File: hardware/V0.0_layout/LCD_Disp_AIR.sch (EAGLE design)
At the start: 41 parts, among them IC3 TC10553.3V, J1 12V input, Q1 16MHz, SW1 ENCODER_SW1-PEC12, U1 ATMEGA328P-AU(R), U3 78M05

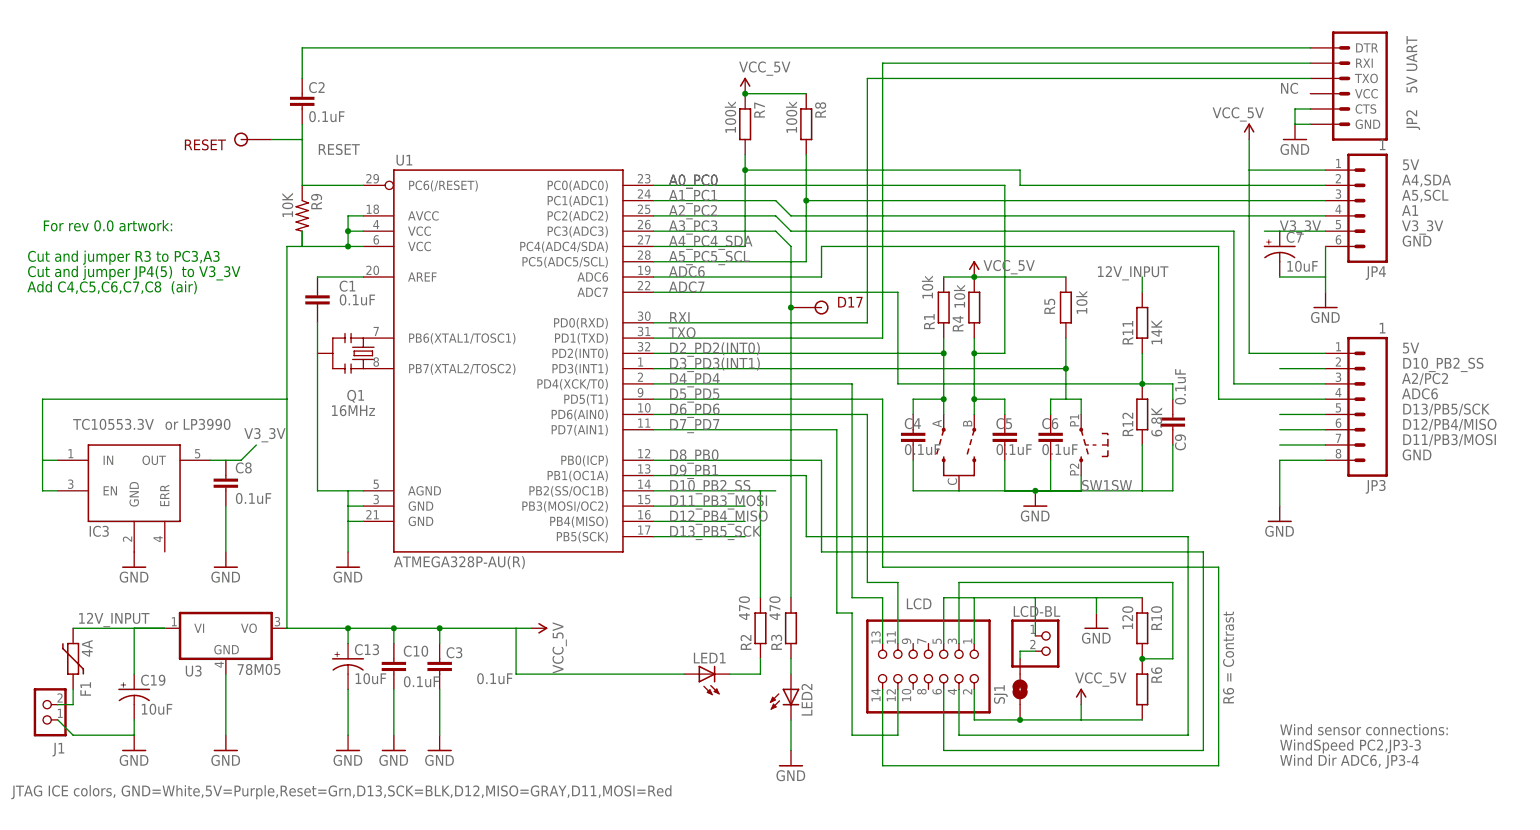
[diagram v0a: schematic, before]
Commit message: added 12_adc_daughter/LTC2495_16x_pga_adc.pdf removed eagle.epf files and added gitignore file
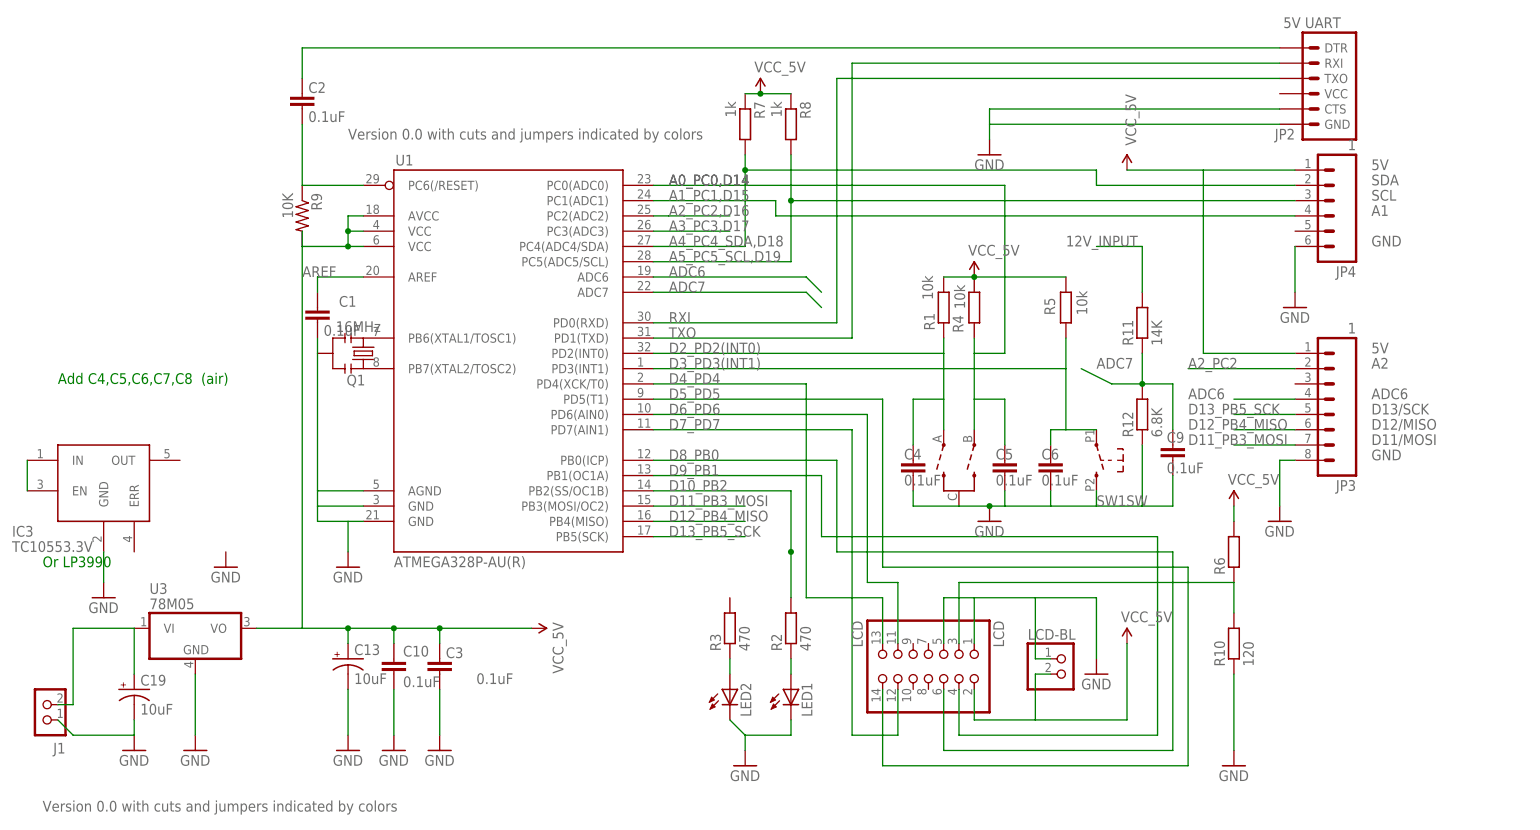
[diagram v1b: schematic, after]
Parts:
- removed C7: 10uF, SparkFun:CAP_POL1206
- removed C8: 0.1uF, SparkFun:CAP0805
- removed D17: D17-A3-PC3, 1AA_Stofer:SOLDER_POINTA
- removed F1: 4A, dp_devices:FUSE_PTC-0805
- removed RESET: SOLDER_POINTA, 1AA_Stofer:SOLDER_POINTA
- removed SJ1: BACKLIGHT, SparkFun-Passives:SOLDERJUMPERNO
- R7, R8: value 100k -> 1k
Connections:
- net A0_PC0 renamed A0_PC0,D14
- net A1_PC1 renamed A1_PC1,D15
- net A4_PC4_SDA renamed A4_PC4_SDA,D18
- net A5_PC5_SCL renamed A5_PC5_SCL,D19
- removed net A3_PC3: D17.P$1, R3.2, U1.PC3(ADC3)
- removed net D10_PB2_SS: JP3.2, R2.2, U1.PB2(SS/OC1B)
- removed net N$11: F1.1, J1.2
- removed net V3_3V: C7.+, C8.1, IC3.OUT, JP4.5
- new net A2_PC2,D16: U1.PC2(ADC2)
- new net A3_PC3,D17: U1.PC3(ADC3)
- new net D10_PB2: R2.2, U1.PB2(SS/OC1B)
- net 12V_INPUT: now also J1.2; no longer F1.2
- net 5V: now also LCD-BL.2; no longer IC3.EN, IC3.IN, LED1.A, SJ1.1
- net A2_PC2: now also JP3.2; no longer JP3.3, U1.PC2(ADC2)
- net GND: now also LED1.C; no longer C7.-, C8.2
- net N$12: now also IC3.EN, IC3.IN; no longer LED1.C, R2.1
- net N$13: now also LED1.A, R2.1; no longer LCD-BL.2, SJ1.2
- net RESET: no longer RESET.P$1
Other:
- note added: "A2"
- note added: "Cut trace"
- note added: "D11/MOSI"
- note added: "D12/MISO"
- note added: "D13/SCK"
- note added: "High wire"
- note added: "Or LP3990"
- note added: "SCL"
- note added: "SDA"
- note added: "Version 0.0 with cuts and jumpers indicated by colors"
- note removed: "A2/PC2"
- note removed: "A4,SDA"
- note removed: "A5,SCL"
- note removed: "Cut and jumper JP4(5) to V3_3V"
- note removed: "Cut and jumper R3 to PC3,A3"
- note removed: "D11/PB3/MOSI"
- note removed: "D12/PB4/MISO"
- note removed: "D13/PB5/SCK"
- note removed: "For rev 0.0 artwork:"
- note removed: "JTAG ICE colors, GND=White,5V=Purple,Reset=Grn,D13,SCK=BLK,D12,MISO=GRAY,D11,MOSI=Red"
- note removed: "NC"
- note removed: "R6 = Contrast"
- note removed: "Wind Dir ADC6, JP3-4"
- note removed: "Wind sensor connections:"
- note removed: "WindSpeed PC2,JP3-3"
- note removed: "or LP3990"
- moved on the sheet: C1, C4, C5, C6, C9, IC3, JP2, JP3, JP4, LCD-BL, LED1, LED2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
